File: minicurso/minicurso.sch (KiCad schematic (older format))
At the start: 17 parts, among them J1 USB_B_Mini, J2 Conn_01x10, J3 Conn_01x10, J4 Conn_01x06, SW1 SW_Push, U1 ATmega32U4-AU, Y1 16MHz

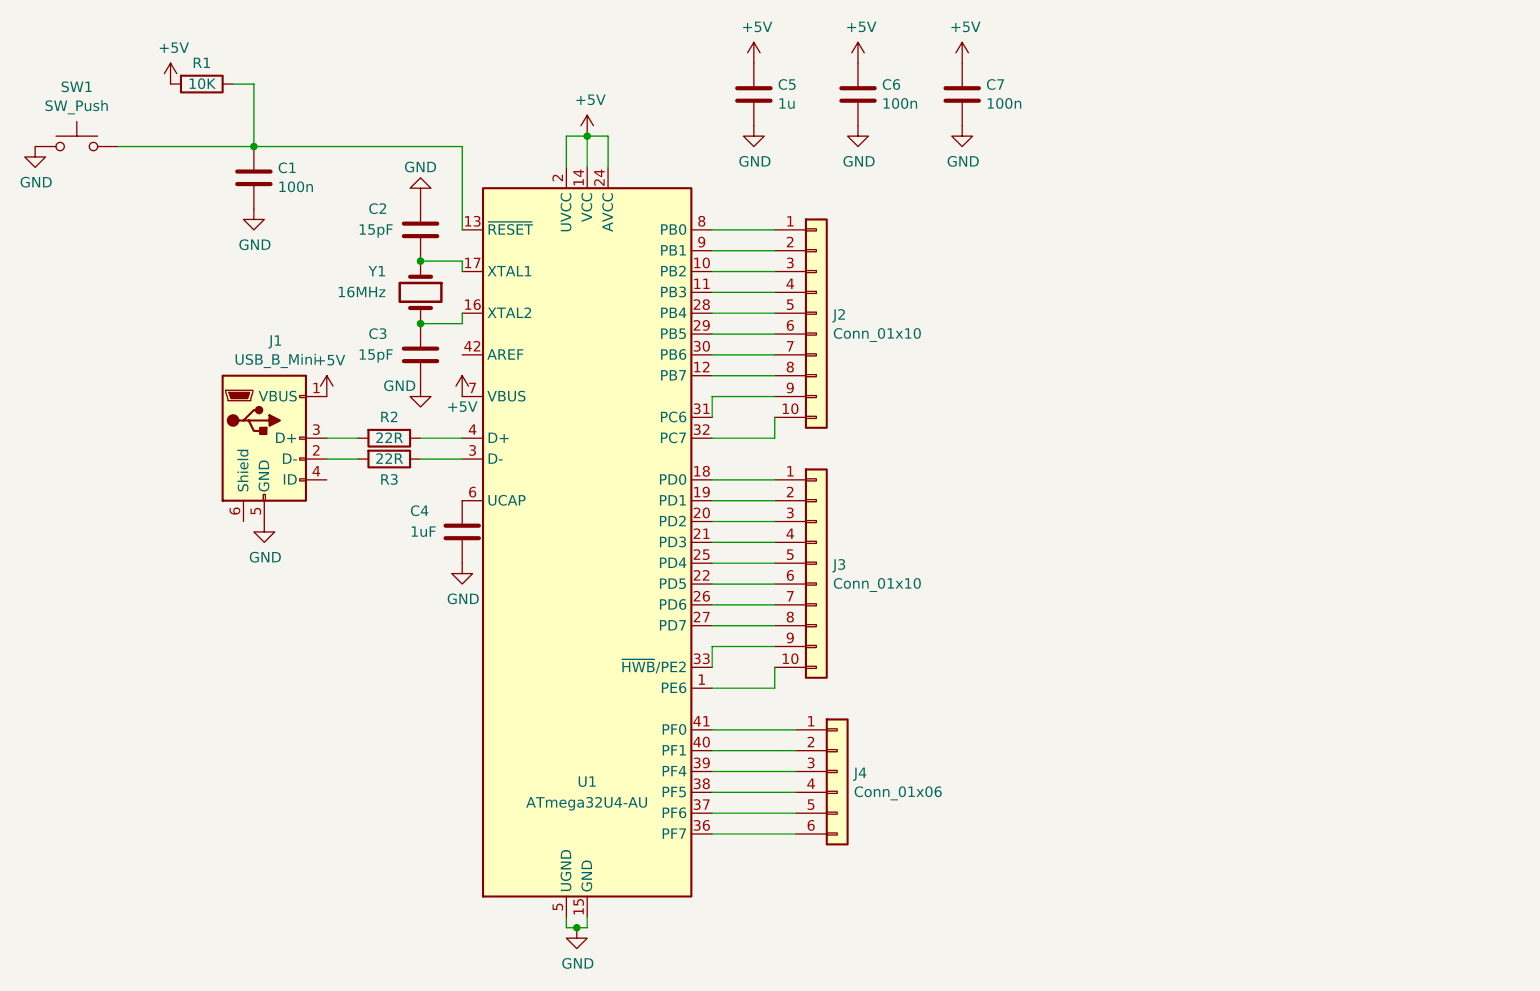
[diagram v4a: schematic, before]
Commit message: Usando label para facilitar desenho
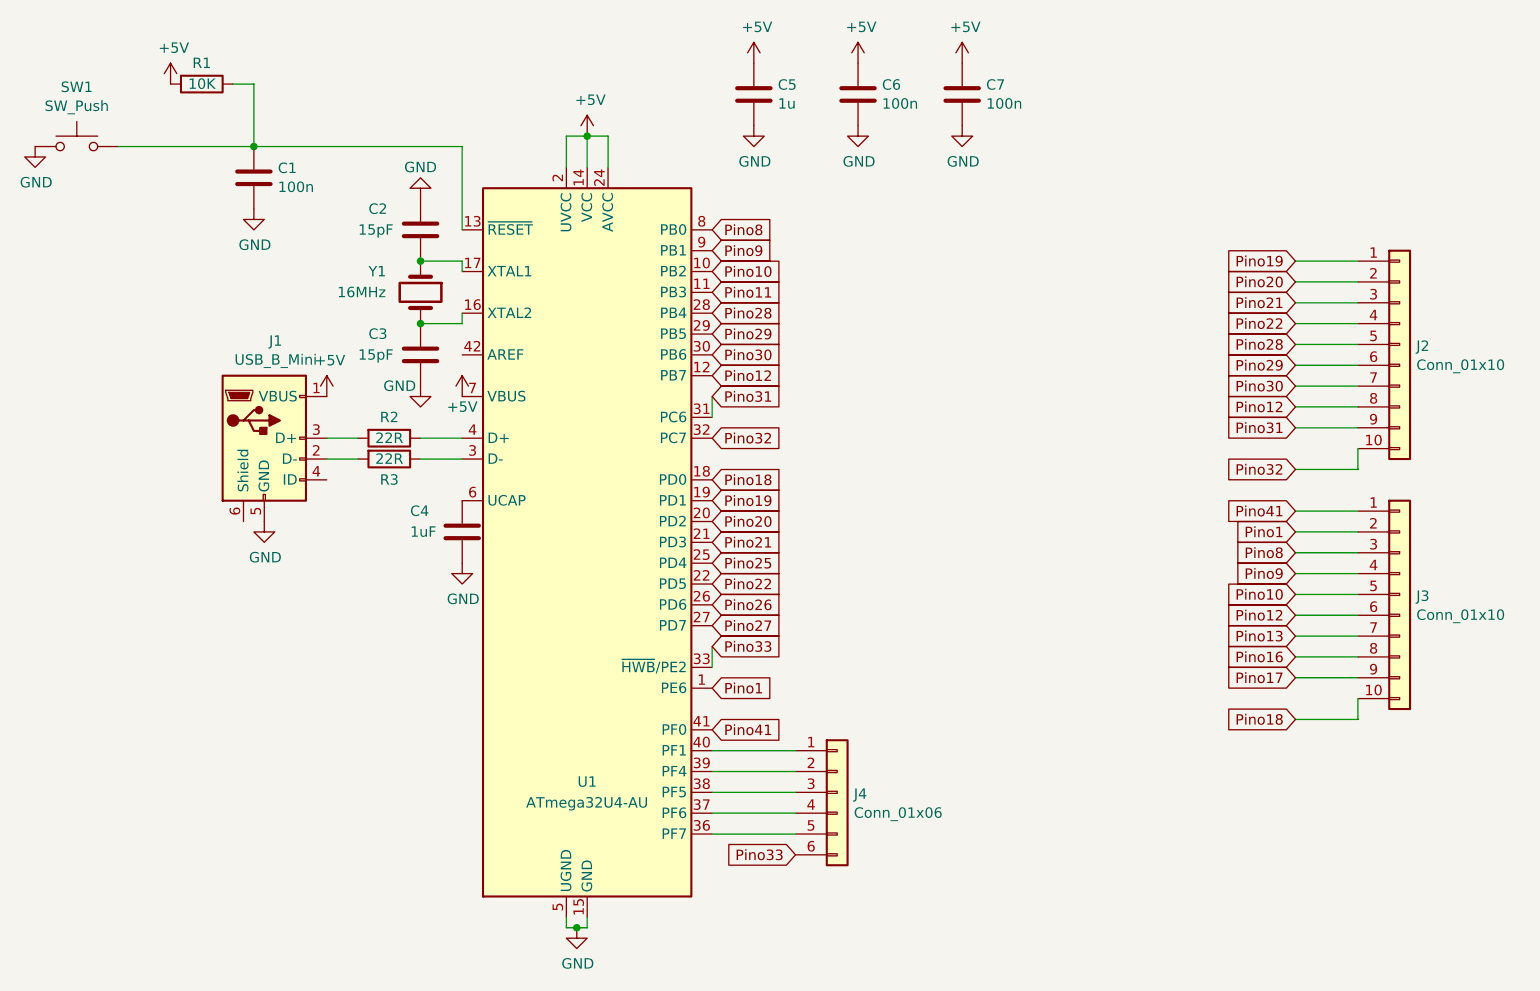
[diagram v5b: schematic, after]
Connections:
- net Pino1: now reaches U1.1 (PE6)
- net Pino1: now also J3.2 (Pin_2); no longer J3.10 (Pin_10)
- net Pino10: now reaches U1.10 (PB2)
- net Pino10: now also J3.5 (Pin_5); no longer J2.3 (Pin_3)
- net Pino11: now reaches U1.11 (PB3)
- net Pino11: no longer J2.4 (Pin_4)
- net Pino12: now reaches J2.8 (Pin_8), U1.12 (PB7)
- net Pino12: now also J3.6 (Pin_6)
- net Pino18: now reaches U1.18 (PD0)
- net Pino18: now also J3.10 (Pin_10); no longer J3.1 (Pin_1)
- net Pino19: now reaches U1.19 (PD1)
- net Pino19: now also J2.1 (Pin_1); no longer J3.2 (Pin_2)
- net Pino20: now reaches U1.20 (PD2)
- net Pino20: now also J2.2 (Pin_2); no longer J3.3 (Pin_3)
- net Pino21: now reaches U1.21 (PD3)
- net Pino21: now also J2.3 (Pin_3); no longer J3.4 (Pin_4)
- net Pino22: now reaches U1.22 (PD5)
- net Pino22: now also J2.4 (Pin_4); no longer J3.6 (Pin_6)
- net Pino25: now reaches U1.25 (PD4)
- net Pino25: no longer J3.5 (Pin_5)
- net Pino13: now reaches J3.7 (Pin_7)
- net Pino13: no longer U1.26 (PD6)
- net Pino16: now reaches J3.8 (Pin_8)
- net Pino16: no longer U1.27 (PD7)
- net Pino28: now reaches J2.5 (Pin_5), U1.28 (PB4)
- net Pino29: now reaches J2.6 (Pin_6), U1.29 (PB5)
- net Pino30: now reaches J2.7 (Pin_7), U1.30 (PB6)
- net Pino31: now reaches J2.9 (Pin_9), U1.31 (PC6)
- net Pino32: now reaches J2.10 (Pin_10), U1.32 (PC7)
- net Pino17: now reaches J3.9 (Pin_9)
- net Pino17: no longer U1.33 (~HWB~/PE2)
- net at U1.36 (PF7): now also J4.5 (Pin_5); no longer J4.6 (Pin_6)
- net at U1.37 (PF6): now also J4.4 (Pin_4); no longer J4.5 (Pin_5)
- net at U1.38 (PF5): now also J4.3 (Pin_3); no longer J4.4 (Pin_4)
- net at U1.39 (PF4): now also J4.2 (Pin_2); no longer J4.3 (Pin_3)
- net at U1.40 (PF1): now also J4.1 (Pin_1); no longer J4.2 (Pin_2)
- net Pino41: now reaches U1.41 (PF0)
- net Pino41: now also J3.1 (Pin_1); no longer J4.1 (Pin_1)
- net Pino8: now reaches U1.8 (PB0)
- net Pino8: now also J3.3 (Pin_3); no longer J2.1 (Pin_1)
- net Pino9: now reaches U1.9 (PB1)
- net Pino9: now also J3.4 (Pin_4); no longer J2.2 (Pin_2)
- new net Pino26: U1.26 (PD6)
- new net Pino27: U1.27 (PD7)
- new net Pino33: J4.6 (Pin_6), U1.33 (~HWB~/PE2)
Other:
- moved on the sheet: J2, J3, J4
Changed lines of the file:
@@
 EESchema Schematic File Version 4
+LIBS:minicurso-cache
 EELAYER 26 0
 EELAYER END
@@
 L Connector_Generic:Conn_01x10 J2
 U 1 1 5D7AB30B
-P 5100 1900
-F 0 "J2" H 5180 1892 50  0000 L CNN
-F 1 "Conn_01x10" H 5180 1801 50  0000 L CNN
-F 2 "Connector_PinHeader_2.54mm:PinHeader_1x10_P2.54mm_Vertical" H 5100 1900 50  0001 C CNN
-F 3 "~" H 5100 1900 50  0001 C CNN
-	1    5100 1900
+P 7900 2050
+F 0 "J2" H 7980 2042 50  0000 L CNN
+F 1 "Conn_01x10" H 7980 1951 50  0000 L CNN
+F 2 "Connector_PinHeader_2.54mm:PinHeader_1x10_P2.54mm_Vertical" H 7900 2050 50  0001 C CNN
+F 3 "~" H 7900 2050 50  0001 C CNN
+	1    7900 2050
 	1    0    0    -1
 $EndComp
@@
 L Connector_Generic:Conn_01x06 J4
 U 1 1 5D7AB549
-P 5200 4100
-F 0 "J4" H 5280 4092 50  0000 L CNN
-F 1 "Conn_01x06" H 5280 4001 50  0000 L CNN
-F 2 "Connector_PinHeader_2.54mm:PinHeader_1x06_P2.54mm_Vertical" H 5200 4100 50  0001 C CNN
-F 3 "~" H 5200 4100 50  0001 C CNN
-	1    5200 4100
+P 5200 4200
+F 0 "J4" H 5280 4192 50  0000 L CNN
+F 1 "Conn_01x06" H 5280 4101 50  0000 L CNN
+F 2 "Connector_PinHeader_2.54mm:PinHeader_1x06_P2.54mm_Vertical" H 5200 4200 50  0001 C CNN
+F 3 "~" H 5200 4200 50  0001 C CNN
+	1    5200 4200
 	1    0    0    -1
 $EndComp
@@
 L Connector_Generic:Conn_01x10 J3
 U 1 1 5D7AB63B
-P 5100 3100
-F 0 "J3" H 5180 3092 50  0000 L CNN
-F 1 "Conn_01x10" H 5180 3001 50  0000 L CNN
-F 2 "Connector_PinHeader_2.54mm:PinHeader_1x10_P2.54mm_Vertical" H 5100 3100 50  0001 C CNN
-F 3 "~" H 5100 3100 50  0001 C CNN
-	1    5100 3100
-	1    0    0    -1
-$EndComp
-Wire Wire Line
-	4600 1500 4900 1500
-Wire Wire Line
-	4600 1600 4900 1600
-Wire Wire Line
-	4600 1700 4900 1700
-Wire Wire Line
-	4600 1800 4900 1800
-Wire Wire Line
-	4600 1900 4900 1900
-Wire Wire Line
-	4600 2000 4900 2000
-Wire Wire Line
-	4600 2100 4900 2100
-Wire Wire Line
-	4900 2200 4600 2200
+P 7900 3250
+F 0 "J3" H 7980 3242 50  0000 L CNN
+F 1 "Conn_01x10" H 7980 3151 50  0000 L CNN
+F 2 "Connector_PinHeader_2.54mm:PinHeader_1x10_P2.54mm_Vertical" H 7900 3250 50  0001 C CNN
+F 3 "~" H 7900 3250 50  0001 C CNN
+	1    7900 3250
+	1    0    0    -1
+$EndComp
+Wire Wire Line
+	7400 1650 7700 1650
+Wire Wire Line
+	7400 1750 7700 1750
+Wire Wire Line
+	7400 1850 7700 1850
+Wire Wire Line
+	7400 1950 7700 1950
+Wire Wire Line
+	7400 2050 7700 2050
+Wire Wire Line
+	7400 2150 7700 2150
+Wire Wire Line
+	7400 2250 7700 2250
+Wire Wire Line
+	7700 2350 7400 2350
 Wire Wire Line
 	4600 2400 4600 2300
 Wire Wire Line
-	4600 2300 4900 2300
-Wire Wire Line
-	4600 2500 4900 2500
-Wire Wire Line
-	4900 2500 4900 2400
-Wire Wire Line
-	4600 2700 4900 2700
-Wire Wire Line
-	4600 2800 4900 2800
-Wire Wire Line
-	4600 2900 4900 2900
-Wire Wire Line
-	4600 3000 4900 3000
-Wire Wire Line
-	4600 3100 4900 3100
-Wire Wire Line
-	4600 3200 4900 3200
-Wire Wire Line
-	4600 3300 4900 3300
-Wire Wire Line
-	4600 3400 4900 3400
+	7400 2450 7700 2450
+Wire Wire Line
+	7400 2650 7700 2650
+Wire Wire Line
+	7700 2650 7700 2550
+Wire Wire Line
+	7400 2950 7700 2950
+Wire Wire Line
+	7400 3050 7700 3050
+Wire Wire Line
+	7400 3150 7700 3150
+Wire Wire Line
+	7400 3250 7700 3250
+Wire Wire Line
+	7400 3350 7700 3350
+Wire Wire Line
+	7400 3450 7700 3450
+Wire Wire Line
+	7400 3550 7700 3550
 Wire Wire Line
 	4600 3600 4600 3500
 Wire Wire Line
-	4600 3500 4900 3500
-Wire Wire Line
-	4600 3700 4900 3700
-Wire Wire Line
-	4900 3700 4900 3600
-Wire Wire Line
-	4600 3900 5000 3900
-Wire Wire Line
-	4600 4000 5000 4000
-Wire Wire Line
-	5000 4100 4600 4100
+	7400 3650 7700 3650
+Wire Wire Line
+	7400 3850 7700 3850
+Wire Wire Line
+	7700 3850 7700 3750
+Wire Wire Line
+	4600 4100 5000 4100
 Wire Wire Line
 	4600 4200 5000 4200
@@
 	1    0    0    -1
 $EndComp
+Text GLabel 4600 1500 2    50   Input ~ 0
+Pino8
+Text GLabel 4600 1600 2    50   Input ~ 0
+Pino9
+Text GLabel 4600 1700 2    50   Input ~ 0
+Pino10
+Text GLabel 4600 1800 2    50   Input ~ 0
+Pino11
+Text GLabel 4600 1900 2    50   Input ~ 0
+Pino28
+Text GLabel 4600 2000 2    50   Input ~ 0
+Pino29
+Text GLabel 4600 2100 2    50   Input ~ 0
+Pino30
+Text GLabel 4600 2200 2    50   Input ~ 0
+Pino12
+Text GLabel 7400 2350 0    50   Input ~ 0
+Pino12
+Text GLabel 7400 2250 0    50   Input ~ 0
+Pino30
+Text GLabel 7400 2150 0    50   Input ~ 0
+Pino29
+Text GLabel 7400 2050 0    50   Input ~ 0
+Pino28
+Text GLabel 7400 1950 0    50   Input ~ 0
+Pino22
+Text GLabel 7400 1850 0    50   Input ~ 0
+Pino21
+Text GLabel 7400 1750 0    50   Input ~ 0
+Pino20
+Text GLabel 7400 1650 0    50   Input ~ 0
+Pino19
+Text GLabel 4600 3700 2    50   Input ~ 0
+Pino1
+Text GLabel 7400 2850 0    50   Input ~ 0
+Pino41
+Text GLabel 7400 2450 0    50   Input ~ 0
+Pino31
+Text GLabel 4600 2300 2    50   Input ~ 0
+Pino31
+Text GLabel 4600 2500 2    50   Input ~ 0
+Pino32
+Text GLabel 7400 2650 0    50   Input ~ 0
+Pino32
+Text GLabel 4600 2700 2    50   Input ~ 0
+Pino18
+Text GLabel 4600 2800 2    50   Input ~ 0
+Pino19
+Text GLabel 4600 2900 2    50   Input ~ 0
+Pino20
+Text GLabel 4600 3000 2    50   Input ~ 0
+Pino21
+Text GLabel 4600 3100 2    50   Input ~ 0
+Pino25
+Text GLabel 4600 3200 2    50   Input ~ 0
+Pino22
+Text GLabel 4600 3300 2    50   Input ~ 0
+Pino26
+Text GLabel 4600 3400 2    50   Input ~ 0
+Pino27
+Text GLabel 4600 3500 2    50   Input ~ 0
+Pino33
+Text GLabel 7400 3850 0    50   Input ~ 0
+Pino18
+Text GLabel 7400 3650 0    50   Input ~ 0
+Pino17
+Text GLabel 7400 3550 0    50   Input ~ 0
+Pino16
+Text GLabel 7400 3450 0    50   Input ~ 0
+Pino13
+Text GLabel 7400 3350 0    50   Input ~ 0
+Pino12
+Text GLabel 7400 3250 0    50   Input ~ 0
+Pino10
+Text GLabel 7400 3150 0    50   Input ~ 0
+Pino9
+Text GLabel 7400 3050 0    50   Input ~ 0
+Pino8
+Text GLabel 7400 2950 0    50   Input ~ 0
+Pino1
+Wire Wire Line
+	4600 4000 5000 4000
+Wire Wire Line
+	7400 2850 7700 2850
+Text GLabel 4600 3900 2    50   Input ~ 0
+Pino41
+Text GLabel 5000 4500 0    50   Input ~ 0
+Pino33
 $EndSCHEMATC
